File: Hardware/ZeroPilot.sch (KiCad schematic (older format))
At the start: 3 parts, among them J1 CONN_01X04

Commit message: Fixed merge issues
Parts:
- removed J1: CONN_01X04, Pin_Headers:Pin_Header_Straight_1x04_Pitch2.54mm, symbol Conn_01x04
- added TP27, TP28, TP29: TEST, symbol TEST
- renumbered TP3 to TP1, TP4 to TP2
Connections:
- net labels removed: 5V_EXT, PW_GOOD_EXT, PW_GOOD_INT
- wire segments 109 -> 104
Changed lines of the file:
@@
 LIBS:contrib
 LIBS:valves
+LIBS:ZeroPilot-cache
 EELAYER 25 0
 EELAYER END
@@
 F48 "SPI4_SCK" B L 7200 5900 60
 F49 "SPI4_MOSI" B L 7200 6100 60
-F50 "PW_GOOD_EXT" I R 8950 5700 60
-F51 "PW_GOOD_INT" I R 8950 5800 60
 F52 "MEM_WC" I R 8950 5600 60
 $EndSheet
@@
 Text Label 1600 2350 0    60   ~ 0
 6V_EXT
-Text Label 7350 1650 2    60   ~ 0
-5V_EXT
+Text Label 6450 1600 2    60   ~ 0
+6V_EXT
 Text Label 8950 5200 0    60   ~ 0
 ULTRA_SONIC_1
@@
 F18 "V_SPK" I L 3550 700 60
 $EndSheet
-Text Label 8950 5700 0    60   ~ 0
-PW_GOOD_EXT
-Text Label 8950 5800 0    60   ~ 0
-PW_GOOD_INT
 $Sheet
 S 4350 6250 1300 1300
@@
 Text Label 6950 3900 0    60   ~ 0
 RTS4
-Text Label 3200 1050 0    60   ~ 0
+Text Label 3550 1050 2    60   ~ 0
 PPM
 Text Label 3150 1650 0    60   ~ 0
@@
 Text Label 3200 3250 0    59   ~ 0
 RX3
-Text Label 3550 850  2    59   ~ 0
+Text Label 3550 1250 2    59   ~ 0
 SAFETY_DBG_RX
 Text Label 3150 3450 0    59   ~ 0
@@
 5V_INT
 Text Label 3150 4300 0    59   ~ 0
-5V_EXT
+6V_EXT
 Text Label 3150 4200 0    59   ~ 0
 5V_INT
@@
 SCLK_SAFETY
 $Comp
-L Conn_01x04 J1
-U 1 1 594DE28B
-P 10450 2800
-F 0 "J1" H 10450 3050 50  0000 C CNN
-F 1 "CONN_01X04" V 10550 2800 50  0000 C CNN
-F 2 "Pin_Headers:Pin_Header_Straight_1x04_Pitch2.54mm" H 10450 2800 50  0001 C CNN
-F 3 "" H 10450 2800 50  0001 C CNN
-F 4 "CONN-008" H 10450 2800 60  0001 C CNN "part_num"
-	1    10450 2800
-	1    0    0    1
-$EndComp
-$Comp
-L GND #PWR1
-U 1 1 594DF6EB
-P 10150 3000
-F 0 "#PWR1" H 10150 2750 50  0001 C CNN
-F 1 "GND" H 10150 2850 50  0000 C CNN
-F 2 "" H 10150 3000 50  0001 C CNN
-F 3 "" H 10150 3000 50  0001 C CNN
-	1    10150 3000
-	1    0    0    -1
-$EndComp
-$Comp
-L GND #PWR2
+L GND #PWR01
 U 1 1 594F2D3B
 P 12300 5850
-F 0 "#PWR2" H 12300 5600 50  0001 C CNN
+F 0 "#PWR01" H 12300 5600 50  0001 C CNN
 F 1 "GND" H 12300 5700 50  0000 C CNN
 F 2 "" H 12300 5850 50  0001 C CNN
@@
 $EndComp
 $Comp
-L PWR_FLAG #FLG1
+L PWR_FLAG #FLG02
 U 1 1 594F3124
 P 12300 5850
-F 0 "#FLG1" H 12300 5925 50  0001 C CNN
+F 0 "#FLG02" H 12300 5925 50  0001 C CNN
 F 1 "PWR_FLAG" H 12300 6000 50  0000 C CNN
 F 2 "" H 12300 5850 50  0001 C CNN
@@
 I2C1: altimeter
 $Comp
-L TEST TP3
+L TEST TP1
 U 1 1 5B17AD8A
 P 4550 4875
-F 0 "TP3" H 4550 5175 50  0000 C BNN
+F 0 "TP1" H 4550 5175 50  0000 C BNN
 F 1 "TEST" H 4550 5125 50  0000 C CNN
 F 2 "" H 4550 4875 50  0001 C CNN
@@
 $EndComp
 $Comp
-L TEST TP4
+L TEST TP2
 U 1 1 5B17B9D1
 P 4550 5080
-F 0 "TP4" H 4550 5380 50  0000 C BNN
+F 0 "TP2" H 4550 5380 50  0000 C BNN
 F 1 "TEST" H 4550 5330 50  0000 C CNN
 F 2 "" H 4550 5080 50  0001 C CNN
@@
 	8950 4400 9650 4400
 Wire Wire Line
-	8950 5500 9300 5500
-Wire Wire Line
 	8950 5600 9300 5600
 Wire Wire Line
-	8950 5700 9550 5700
-Wire Wire Line
-	8950 5800 9550 5800
-Wire Wire Line
 	4350 6800 4000 6800
 Wire Wire Line
@@
 	3150 4650 3550 4650
 Wire Wire Line
-	8950 2700 10250 2700
-Wire Wire Line
-	8950 2800 10250 2800
-Wire Wire Line
-	9650 2900 10250 2900
-Wire Wire Line
-	10250 3000 10150 3000
-Wire Wire Line
-	10150 3000 10150 3100
+	8950 2800 10500 2800
+Wire Wire Line
+	9650 2900 10600 2900
 Wire Wire Line
 	9900 4050 8950 4050
@@
 Text Label 1600 1200 0    60   ~ 0
 5V_USB
+$Comp
+L TEST TP27
+U 1 1 5B375115
+P 10350 2700
+F 0 "TP27" H 10350 3000 50  0000 C BNN
+F 1 "TEST" H 10350 2950 50  0000 C CNN
+F 2 "" H 10350 2700 50  0001 C CNN
+F 3 "" H 10350 2700 50  0001 C CNN
+	1    10350 2700
+	1    0    0    -1
+$EndComp
+$Comp
+L TEST TP28
+U 1 1 5B375EC5
+P 10500 2800
+F 0 "TP28" H 10500 3100 50  0000 C BNN
+F 1 "TEST" H 10500 3050 50  0000 C CNN
+F 2 "" H 10500 2800 50  0001 C CNN
+F 3 "" H 10500 2800 50  0001 C CNN
+	1    10500 2800
+	1    0    0    -1
+$EndComp
+$Comp
+L TEST TP29
+U 1 1 5B37635D
+P 10600 2900
+F 0 "TP29" H 10600 3200 50  0000 C BNN
+F 1 "TEST" H 10600 3150 50  0000 C CNN
+F 2 "" H 10600 2900 50  0001 C CNN
+F 3 "" H 10600 2900 50  0001 C CNN
+	1    10600 2900
+	1    0    0    -1
+$EndComp
+Wire Wire Line
+	10350 2700 8950 2700
 $EndSCHEMATC

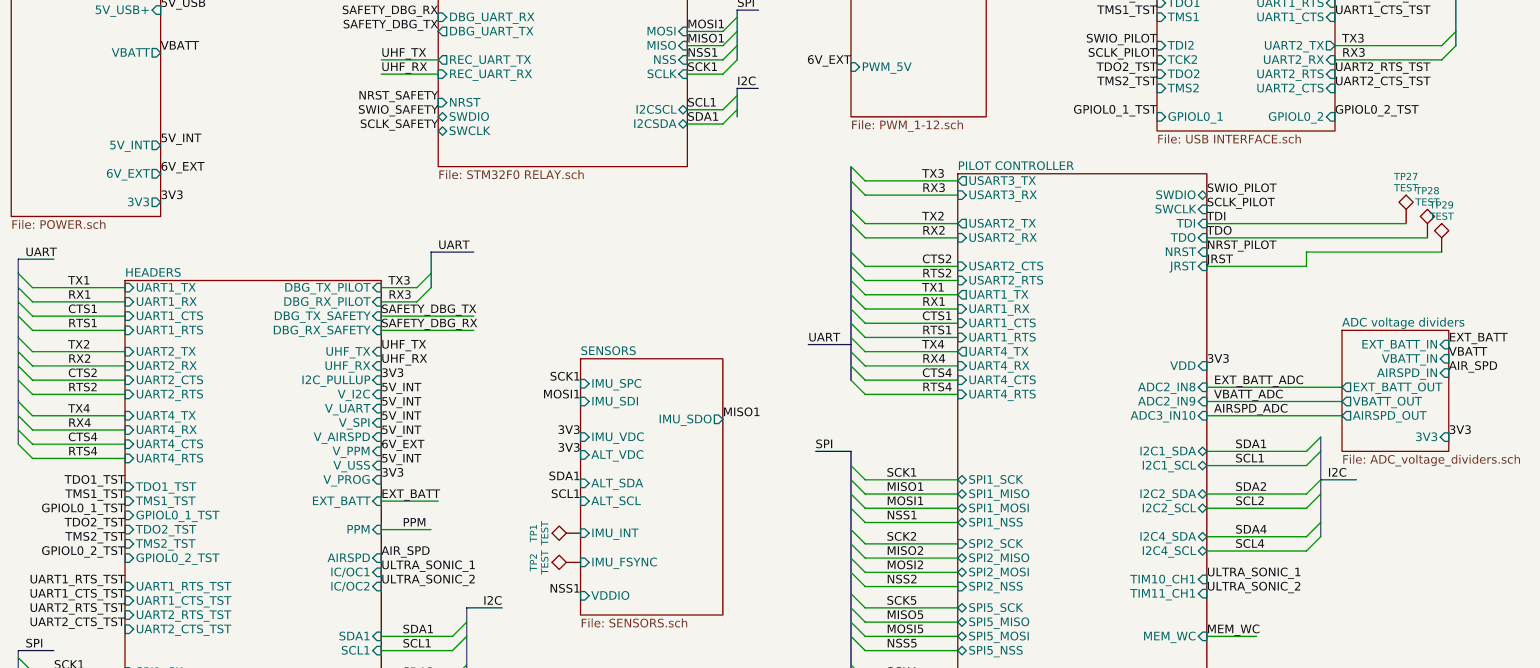
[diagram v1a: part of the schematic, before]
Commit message: USB Interface REV1 (#13)
* Connected NRST pins to USB Interface

Connected the MCUs NRST pins to the GPIO0 pins on the A and B channels of the FT4232H. Also deleted the redundant test points resulting from this.

* Updated Resistors

Changed 1K resistors on DBUS1 lines to 220R resistors and 100R resistors on DBUS2 lines to 0R resistors, on the FT4232H.

* Deleted Old TPs

* Fixed Bugs

Noticed my part numbers in the library had been overwritten, so updated to reflect adding them back with new numbers. Also fixed typo with TVS diodes.

* Fixed one more bug

Fixed overwritten part num
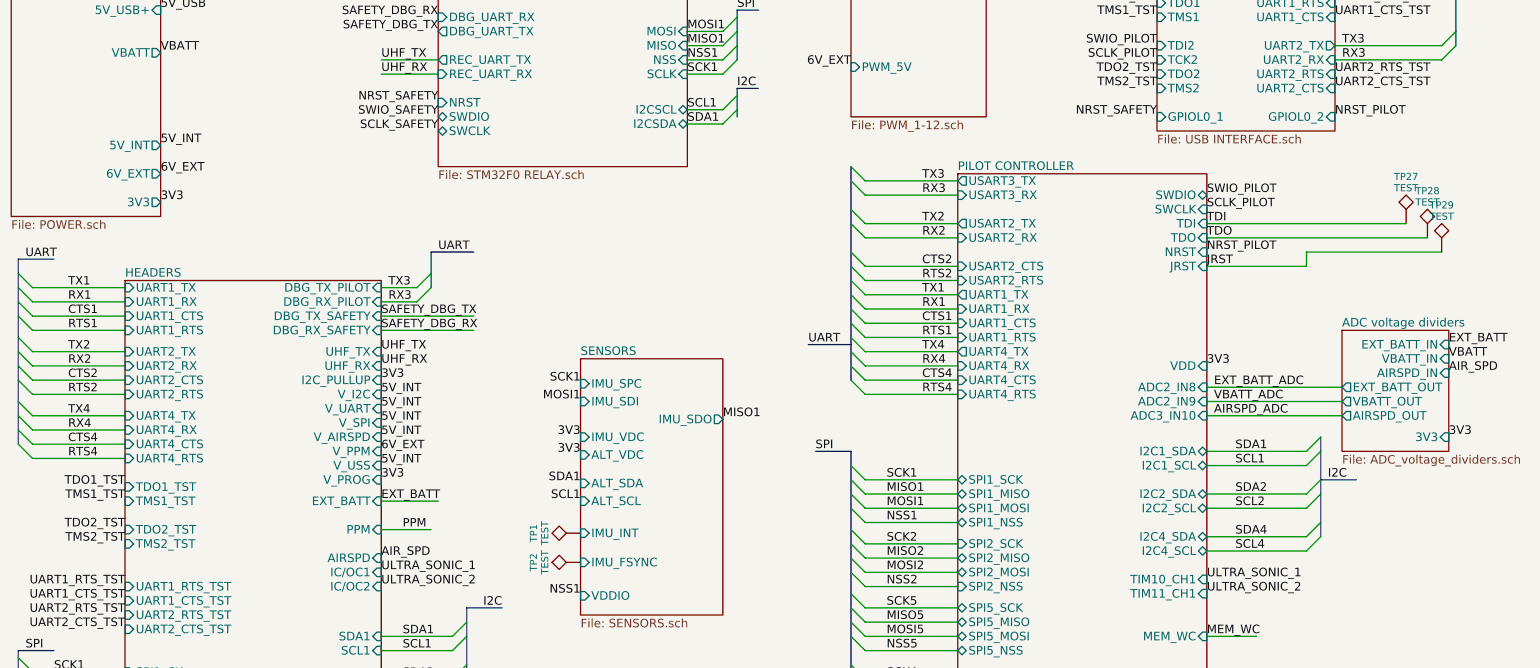
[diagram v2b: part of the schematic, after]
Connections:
- net labels removed: GPIOL0_1_TST, GPIOL0_2_TST
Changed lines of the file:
@@
 TMS2_TST
 Text Label 8600 1950 2    60   ~ 0
-GPIOL0_1_TST
+NRST_SAFETY
 Text Label 9850 1950 0    60   ~ 0
-GPIOL0_2_TST
+NRST_PILOT
 Text Label 9850 1150 0    60   ~ 0
 UART1_RTS_TST
@@
 Text Label 1350 4650 2    60   ~ 0
 TMS1_TST
-Text Label 1350 4750 2    60   ~ 0
-GPIOL0_1_TST
 Text Label 1350 4850 2    60   ~ 0
 TDO2_TST
 Text Label 1350 4950 2    60   ~ 0
 TMS2_TST
-Text Label 1350 5050 2    60   ~ 0
-GPIOL0_2_TST
 $Sheet
 S 1350 3100 1800 4500
@@
 F61 "TDO1_TST" I L 1350 4550 60
 F62 "TMS1_TST" I L 1350 4650 60
-F63 "GPIOL0_1_TST" I L 1350 4750 60
-F64 "TDO2_TST" I L 1350 4850 60
-F65 "TMS2_TST" I L 1350 4950 60
-F66 "GPIOL0_2_TST" I L 1350 5050 60
-F67 "UART1_RTS_TST" I L 1350 5250 60
-F68 "UART1_CTS_TST" I L 1350 5350 60
-F69 "UART2_RTS_TST" I L 1350 5450 60
-F70 "UART2_CTS_TST" I L 1350 5550 60
+F63 "TDO2_TST" I L 1350 4850 60
+F64 "TMS2_TST" I L 1350 4950 60
+F65 "UART1_RTS_TST" I L 1350 5250 60
+F66 "UART1_CTS_TST" I L 1350 5350 60
+F67 "UART2_RTS_TST" I L 1350 5450 60
+F68 "UART2_CTS_TST" I L 1350 5550 60
 $EndSheet
 Text Label 1350 5250 2    60   ~ 0

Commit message: Revert "Add files via upload"
This reverts commit 5604160992b0e2f63895336bcd07dee2b13465c5.
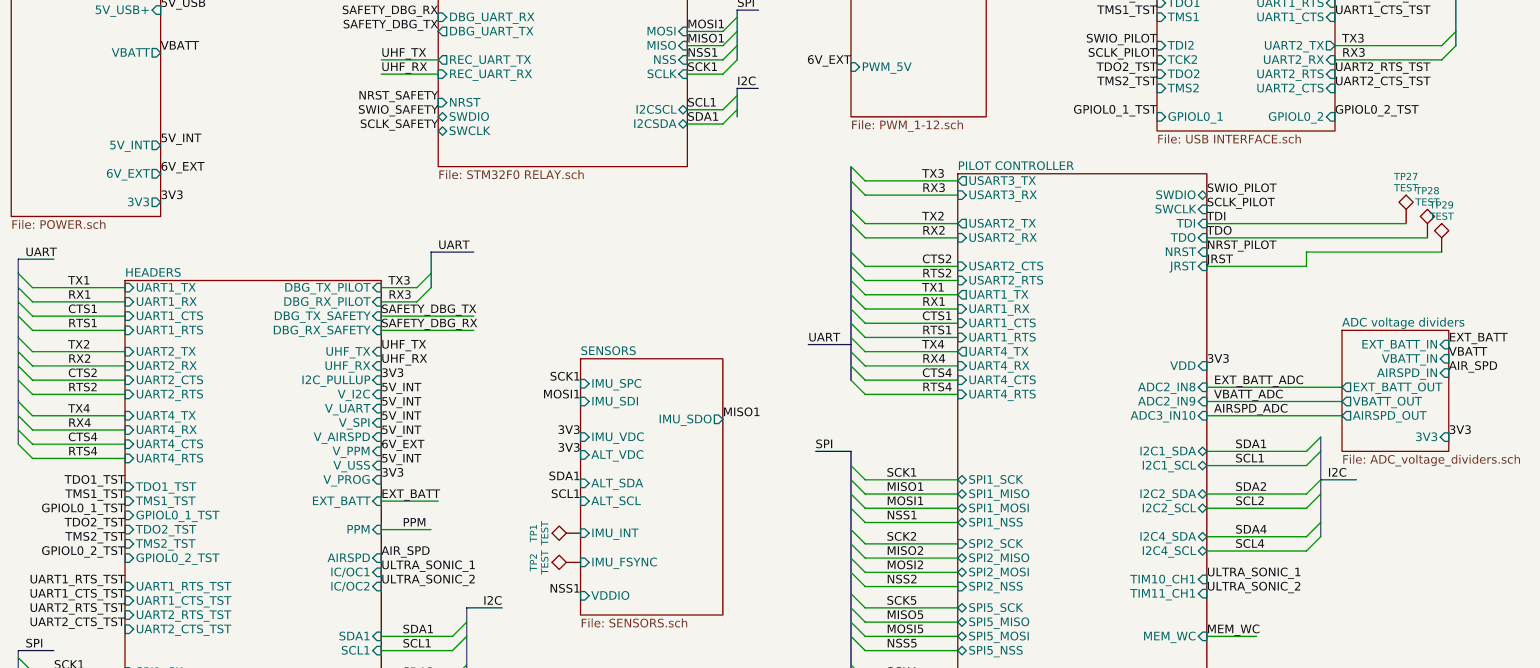
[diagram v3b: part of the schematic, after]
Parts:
- TP1, TP2, TP27, TP28, TP29: footprint (none) -> Measurement_Points:Measurement_Point_Round-SMD-Pad_Small
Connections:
- net labels added: GPIOL0_1_TST, GPIOL0_2_TST
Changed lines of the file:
@@
 F48 "SPI4_SCK" B L 7200 5900 60
 F49 "SPI4_MOSI" B L 7200 6100 60
-F52 "MEM_WC" I R 8950 5600 60
+F50 "MEM_WC" I R 8950 5600 60
 $EndSheet
 Text Label 3550 850  2    60   ~ 0
@@
 SCLK_SAFETY
 $Comp
-L GND #PWR01
+L GND #PWR1
 U 1 1 594F2D3B
 P 12300 5850
-F 0 "#PWR01" H 12300 5600 50  0001 C CNN
+F 0 "#PWR1" H 12300 5600 50  0001 C CNN
 F 1 "GND" H 12300 5700 50  0000 C CNN
 F 2 "" H 12300 5850 50  0001 C CNN
@@
 $EndComp
 $Comp
-L PWR_FLAG #FLG02
+L PWR_FLAG #FLG1
 U 1 1 594F3124
 P 12300 5850
-F 0 "#FLG02" H 12300 5925 50  0001 C CNN
+F 0 "#FLG1" H 12300 5925 50  0001 C CNN
 F 1 "PWR_FLAG" H 12300 6000 50  0000 C CNN
 F 2 "" H 12300 5850 50  0001 C CNN
@@
 F 0 "TP1" H 4550 5175 50  0000 C BNN
 F 1 "TEST" H 4550 5125 50  0000 C CNN
-F 2 "" H 4550 4875 50  0001 C CNN
+F 2 "Measurement_Points:Measurement_Point_Round-SMD-Pad_Small" H 4550 4875 50  0001 C CNN
 F 3 "" H 4550 4875 50  0001 C CNN
 	1    4550 4875
@@
 F 0 "TP2" H 4550 5380 50  0000 C BNN
 F 1 "TEST" H 4550 5330 50  0000 C CNN
-F 2 "" H 4550 5080 50  0001 C CNN
+F 2 "Measurement_Points:Measurement_Point_Round-SMD-Pad_Small" H 4550 5080 50  0001 C CNN
 F 3 "" H 4550 5080 50  0001 C CNN
 	1    4550 5080
@@
 TMS2_TST
 Text Label 8600 1950 2    60   ~ 0
-NRST_SAFETY
+GPIOL0_1_TST
 Text Label 9850 1950 0    60   ~ 0
-NRST_PILOT
+GPIOL0_2_TST
 Text Label 9850 1150 0    60   ~ 0
 UART1_RTS_TST
@@
 Text Label 1350 4650 2    60   ~ 0
 TMS1_TST
+Text Label 1350 4750 2    60   ~ 0
+GPIOL0_1_TST
 Text Label 1350 4850 2    60   ~ 0
 TDO2_TST
 Text Label 1350 4950 2    60   ~ 0
 TMS2_TST
+Text Label 1350 5050 2    60   ~ 0
+GPIOL0_2_TST
 $Sheet
 S 1350 3100 1800 4500
@@
 F61 "TDO1_TST" I L 1350 4550 60
 F62 "TMS1_TST" I L 1350 4650 60
-F63 "TDO2_TST" I L 1350 4850 60
-F64 "TMS2_TST" I L 1350 4950 60
-F65 "UART1_RTS_TST" I L 1350 5250 60
-F66 "UART1_CTS_TST" I L 1350 5350 60
-F67 "UART2_RTS_TST" I L 1350 5450 60
-F68 "UART2_CTS_TST" I L 1350 5550 60
+F63 "GPIOL0_1_TST" I L 1350 4750 60
+F64 "TDO2_TST" I L 1350 4850 60
+F65 "TMS2_TST" I L 1350 4950 60
+F66 "GPIOL0_2_TST" I L 1350 5050 60
+F67 "UART1_RTS_TST" I L 1350 5250 60
+F68 "UART1_CTS_TST" I L 1350 5350 60
+F69 "UART2_RTS_TST" I L 1350 5450 60
+F70 "UART2_CTS_TST" I L 1350 5550 60
 $EndSheet
 Text Label 1350 5250 2    60   ~ 0
@@
 F 0 "TP27" H 10350 3000 50  0000 C BNN
 F 1 "TEST" H 10350 2950 50  0000 C CNN
-F 2 "" H 10350 2700 50  0001 C CNN
+F 2 "Measurement_Points:Measurement_Point_Round-SMD-Pad_Small" H 10350 2700 50  0001 C CNN
 F 3 "" H 10350 2700 50  0001 C CNN
 	1    10350 2700
@@
 F 0 "TP28" H 10500 3100 50  0000 C BNN
 F 1 "TEST" H 10500 3050 50  0000 C CNN
-F 2 "" H 10500 2800 50  0001 C CNN
+F 2 "Measurement_Points:Measurement_Point_Round-SMD-Pad_Small" H 10500 2800 50  0001 C CNN
 F 3 "" H 10500 2800 50  0001 C CNN
 	1    10500 2800
@@
 F 0 "TP29" H 10600 3200 50  0000 C BNN
 F 1 "TEST" H 10600 3150 50  0000 C CNN
-F 2 "" H 10600 2900 50  0001 C CNN
+F 2 "Measurement_Points:Measurement_Point_Round-SMD-Pad_Small" H 10600 2900 50  0001 C CNN
 F 3 "" H 10600 2900 50  0001 C CNN
 	1    10600 2900

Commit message: Updated REV1 branch with changes from USB Interface Revision
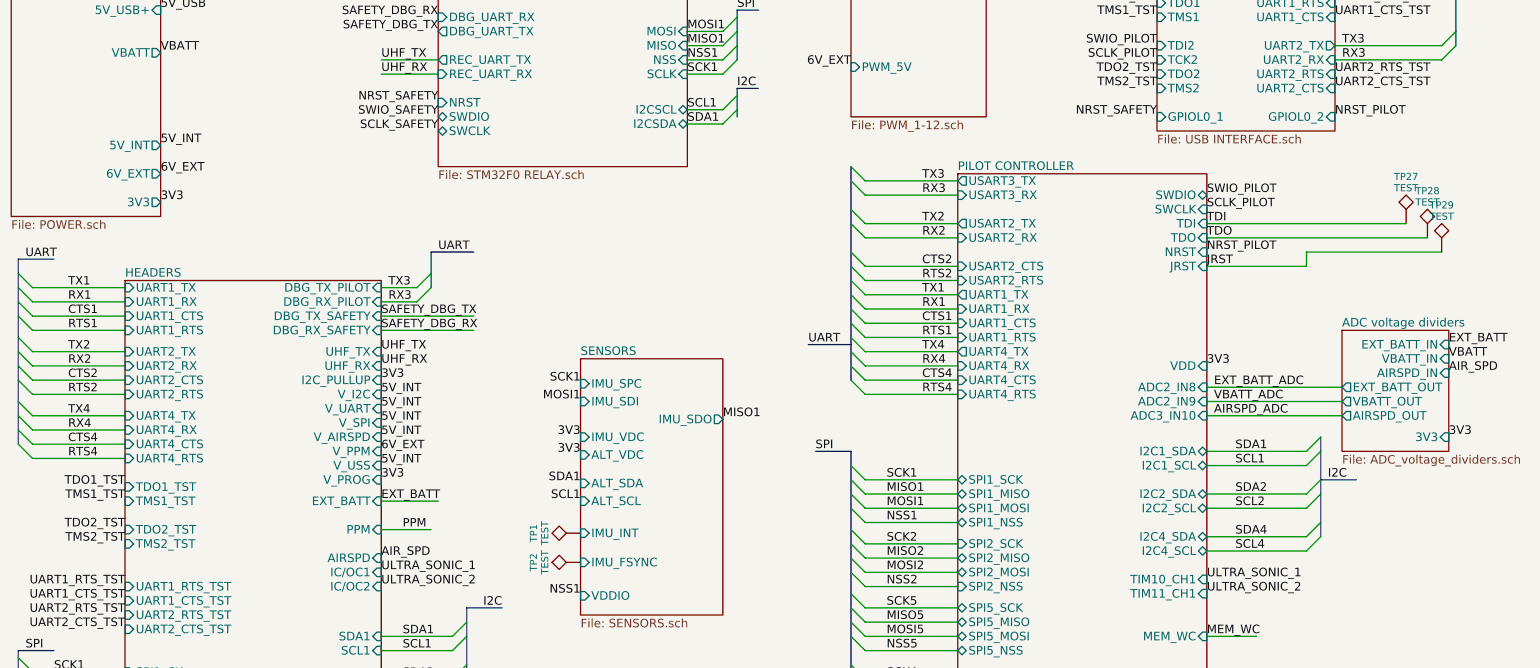
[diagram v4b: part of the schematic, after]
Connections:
- net labels removed: GPIOL0_1_TST, GPIOL0_2_TST
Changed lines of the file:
@@
 Text Label 8600 1750 2    60   ~ 0
 TMS2_TST
-Text Label 8600 1950 2    60   ~ 0
-GPIOL0_1_TST
 Text Label 9850 1950 0    60   ~ 0
-GPIOL0_2_TST
+NRST_PILOT
 Text Label 9850 1150 0    60   ~ 0
 UART1_RTS_TST
@@
 Text Label 1350 4650 2    60   ~ 0
 TMS1_TST
-Text Label 1350 4750 2    60   ~ 0
-GPIOL0_1_TST
 Text Label 1350 4850 2    60   ~ 0
 TDO2_TST
 Text Label 1350 4950 2    60   ~ 0
 TMS2_TST
-Text Label 1350 5050 2    60   ~ 0
-GPIOL0_2_TST
 $Sheet
 S 1350 3100 1800 4500
@@
 F61 "TDO1_TST" I L 1350 4550 60
 F62 "TMS1_TST" I L 1350 4650 60
-F63 "GPIOL0_1_TST" I L 1350 4750 60
-F64 "TDO2_TST" I L 1350 4850 60
-F65 "TMS2_TST" I L 1350 4950 60
-F66 "GPIOL0_2_TST" I L 1350 5050 60
-F67 "UART1_RTS_TST" I L 1350 5250 60
-F68 "UART1_CTS_TST" I L 1350 5350 60
-F69 "UART2_RTS_TST" I L 1350 5450 60
-F70 "UART2_CTS_TST" I L 1350 5550 60
+F63 "TDO2_TST" I L 1350 4850 60
+F64 "TMS2_TST" I L 1350 4950 60
+F65 "UART1_RTS_TST" I L 1350 5250 60
+F66 "UART1_CTS_TST" I L 1350 5350 60
+F67 "UART2_RTS_TST" I L 1350 5450 60
+F68 "UART2_CTS_TST" I L 1350 5550 60
 $EndSheet
 Text Label 1350 5250 2    60   ~ 0
@@
 Wire Wire Line
 	10350 2700 8950 2700
+Text Label 8600 1950 2    60   ~ 0
+NRST_SAFETY
 $EndSCHEMATC
